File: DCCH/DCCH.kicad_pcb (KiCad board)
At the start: 4 copper layers, 139.7 x 88.9 mm, 30 parts, among them J1 Conn_01x02, J2 Conn_01x02, J3 Conn_01x05, J4 Conn_01x05, J5 Conn_02x08_Odd_Even, U11 SN74HC595, U12 SN74HC595, U13 SN74HC595, U14 SN74HC595, U21 SN754410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

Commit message: Added a layer number indicator.
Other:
- board text added: "1"
- board text added: "2"
- board text added: "3"
- board text added: "4"
- board text added: "LAYER"

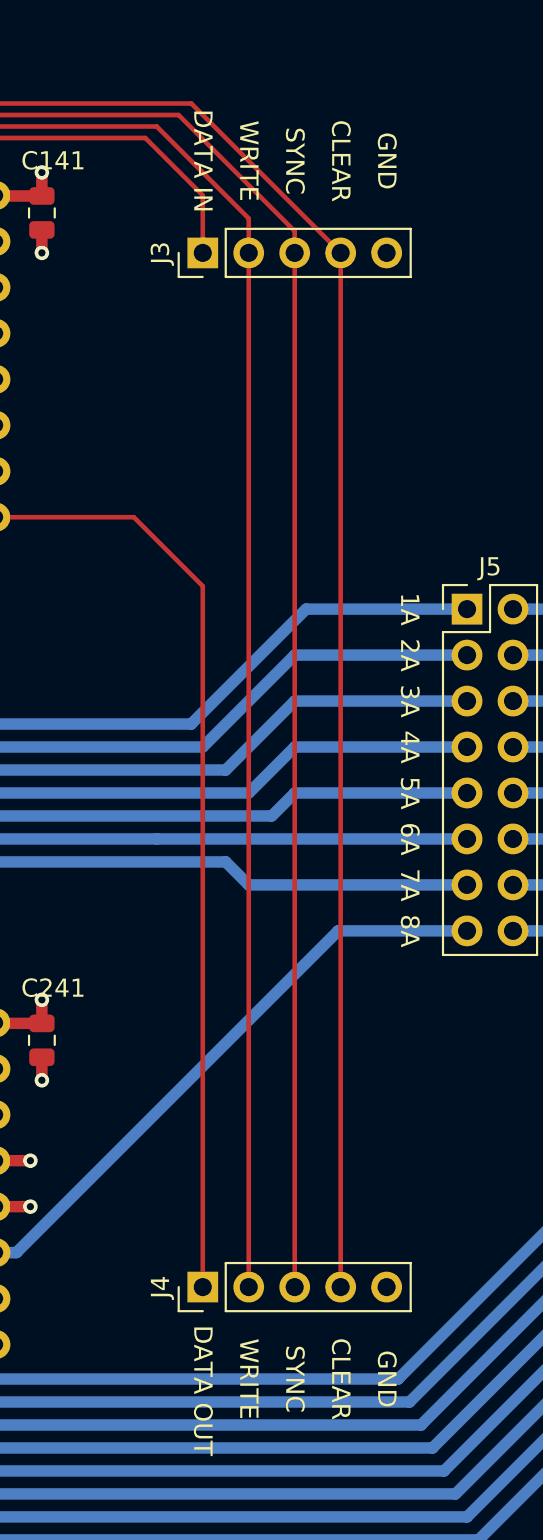
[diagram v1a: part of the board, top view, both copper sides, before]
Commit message: Fixed WRITE and SYNC pins, as they were mixed up.
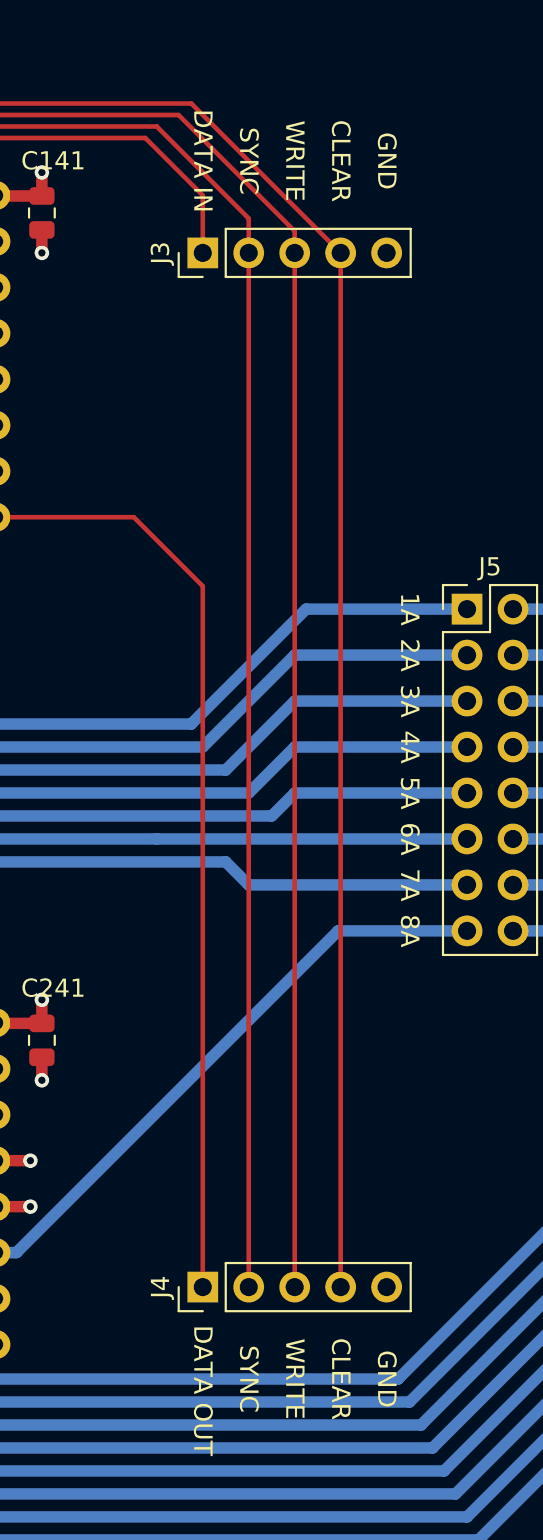
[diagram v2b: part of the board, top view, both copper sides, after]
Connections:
- J3 pad 2: WRITE -> SYNC
- J3 pad 3: SYNC -> WRITE
- J4 pad 2: WRITE -> SYNC
- J4 pad 3: SYNC -> WRITE
- U11 pad 11: SYNC -> WRITE
- U11 pad 12: WRITE -> SYNC
- U12 pad 11: SYNC -> WRITE
- U12 pad 12: WRITE -> SYNC
- U13 pad 11: SYNC -> WRITE
- U13 pad 12: WRITE -> SYNC
- U14 pad 11: SYNC -> WRITE
- U14 pad 12: WRITE -> SYNC
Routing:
- net WRITE: track 211.4 -> 217.5 mm
- net SYNC: track 217.5 -> 211.4 mm

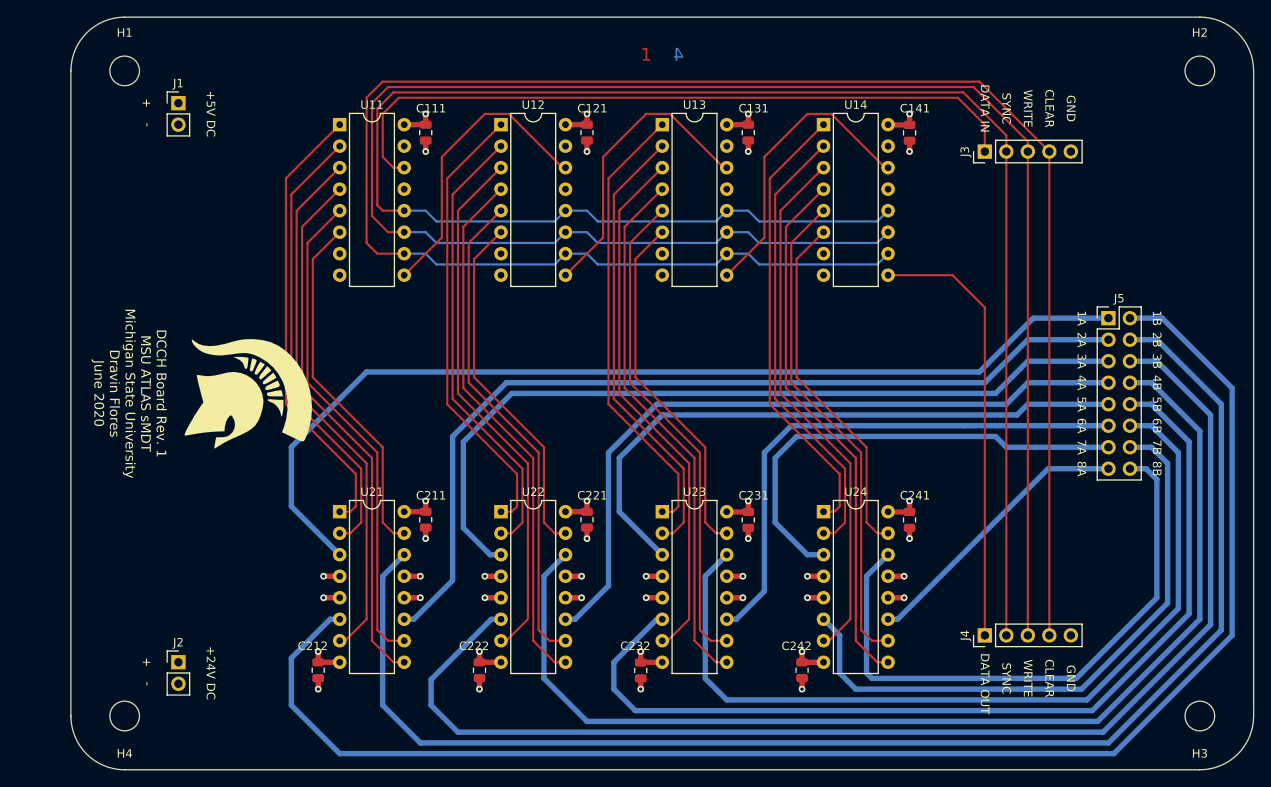
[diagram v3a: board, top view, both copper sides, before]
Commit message: Changed board layout once again. Updated schematic. Updated board.
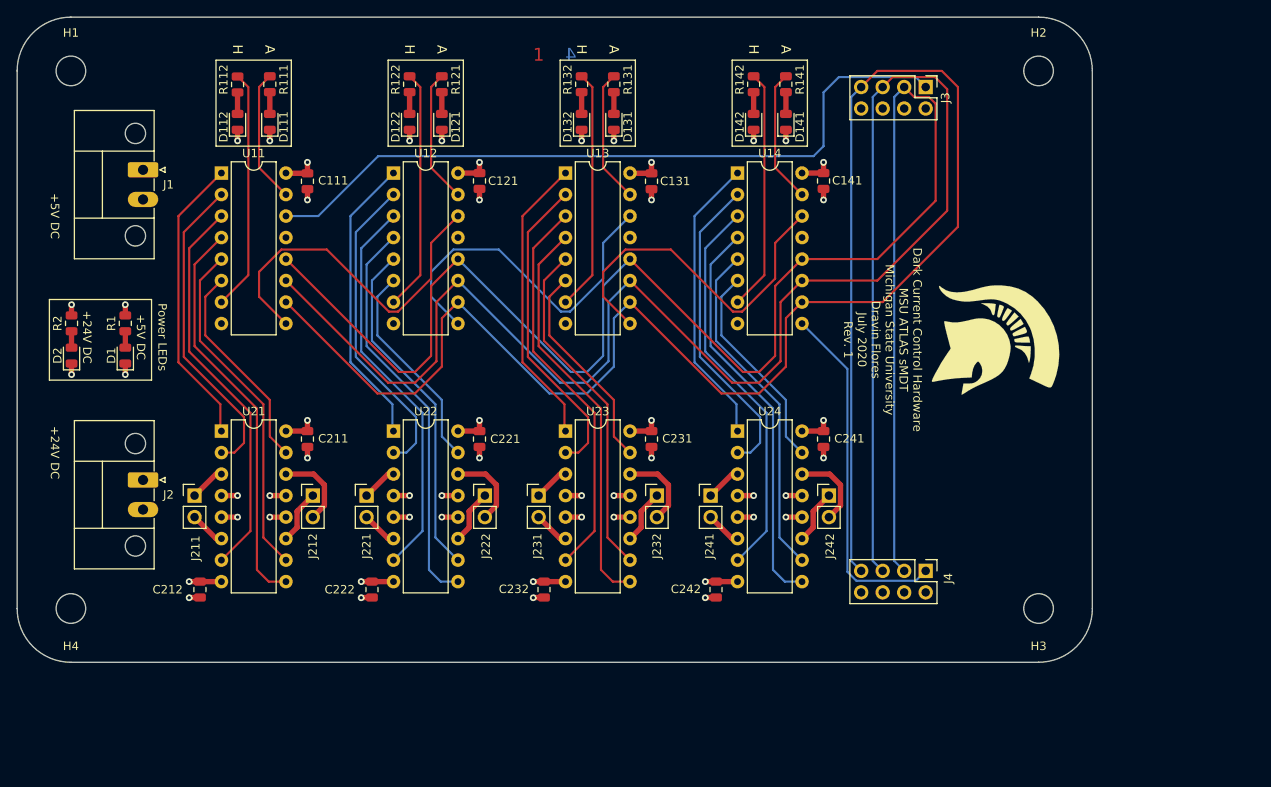
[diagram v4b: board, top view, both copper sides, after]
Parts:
- removed J5: Conn_02x08_Odd_Even, Connector_PinHeader_2.54mm:PinHeader_2x08_P2.54mm_Vertical
- added D1: LED, LED_SMD:LED_0805_2012Metric, F.Cu at (76.3, 78.1)
- added D111: LED, LED_SMD:LED_0805_2012Metric, F.Cu at (93.3, 50.5)
- added D112: LED, LED_SMD:LED_0805_2012Metric, F.Cu at (89.5, 50.5)
- added D121: LED, LED_SMD:LED_0805_2012Metric, F.Cu at (113.7, 50.5)
- added D122: LED, LED_SMD:LED_0805_2012Metric, F.Cu at (109.9, 50.5)
- added D131: LED, LED_SMD:LED_0805_2012Metric, F.Cu at (134.0, 50.5)
- added D132: LED, LED_SMD:LED_0805_2012Metric, F.Cu at (130.2, 50.5)
- added D141: LED, LED_SMD:LED_0805_2012Metric, F.Cu at (154.3, 50.5)
- added D142: LED, LED_SMD:LED_0805_2012Metric, F.Cu at (150.5, 50.5)
- added D2: LED, LED_SMD:LED_0805_2012Metric, F.Cu at (69.9, 78.1)
- added J211: Conn_01x02, Connector_PinHeader_2.54mm:PinHeader_1x02_P2.54mm_Vertical, F.Cu at (84.5, 94.6)
- added J212: Conn_01x02, Connector_PinHeader_2.54mm:PinHeader_1x02_P2.54mm_Vertical, F.Cu at (98.4, 94.6)
- added J221: Conn_01x02, Connector_PinHeader_2.54mm:PinHeader_1x02_P2.54mm_Vertical, F.Cu at (104.8, 94.6)
- added J222: Conn_01x02, Connector_PinHeader_2.54mm:PinHeader_1x02_P2.54mm_Vertical, F.Cu at (118.7, 94.6)
- added J231: Conn_01x02, Connector_PinHeader_2.54mm:PinHeader_1x02_P2.54mm_Vertical, F.Cu at (125.1, 94.6)
- added J232: Conn_01x02, Connector_PinHeader_2.54mm:PinHeader_1x02_P2.54mm_Vertical, F.Cu at (139.1, 94.6)
- added J241: Conn_01x02, Connector_PinHeader_2.54mm:PinHeader_1x02_P2.54mm_Vertical, F.Cu at (145.4, 94.6)
- added J242: Conn_01x02, Connector_PinHeader_2.54mm:PinHeader_1x02_P2.54mm_Vertical, F.Cu at (159.4, 94.6)
- added R1: R_US, Resistor_SMD:R_0805_2012Metric, F.Cu at (76.3, 74.3)
- added R111: R_US, Resistor_SMD:R_0805_2012Metric, F.Cu at (93.3, 46.0)
- added R112: R_US, Resistor_SMD:R_0805_2012Metric, F.Cu at (89.5, 46.1)
- added R121: R_US, Resistor_SMD:R_0805_2012Metric, F.Cu at (113.7, 46.0)
- added R122: R_US, Resistor_SMD:R_0805_2012Metric, F.Cu at (109.9, 46.0)
- added R131: R_US, Resistor_SMD:R_0805_2012Metric, F.Cu at (134.0, 46.0)
- added R132: R_US, Resistor_SMD:R_0805_2012Metric, F.Cu at (130.2, 46.0)
- added R141: R_US, Resistor_SMD:R_0805_2012Metric, F.Cu at (154.3, 46.0)
- added R142: R_US, Resistor_SMD:R_0805_2012Metric, F.Cu at (150.5, 46.0)
- added R2: R_US, Resistor_SMD:R_0805_2012Metric, F.Cu at (69.9, 74.3)
- J1, J2: footprint Connector_PinHeader_2.54mm:PinHeader_1x02_P2.54mm_Vertical -> Connector_Phoenix_MC:PhoenixContact_MC_1,5_2-GF-3.5_1x02_P3.50mm_Horizontal_ThreadedFlange_MountHole
- J3, J4: value Conn_01x05 -> Conn_02x04_Odd_Even; footprint Connector_PinHeader_2.54mm:PinHeader_1x05_P2.54mm_Vertical -> Connector_PinHeader_2.54mm:PinHeader_2x04_P2.54mm_Vertical
- moved G*** 88.5 mm to (179.1, 76.2)
- moved H3 22.9 mm to (184.2, 108.0)
- moved J2 21.9 mm to (78.4, 92.8), turned to 270 degrees
- moved H2 19.0 mm to (184.2, 44.5)
- moved C211 16.9 mm to (97.8, 87.9)
- moved C212 16.9 mm to (85.1, 105.7)
- moved U21 16.9 mm to (87.6, 87.0)
- moved C221 15.9 mm to (118.1, 87.9)
- moved C222 15.9 mm to (105.4, 105.7)
- moved U22 15.9 mm to (108.0, 87.0)
- moved C111 15.1 mm to (97.8, 57.5)
- moved U11 15.1 mm to (87.6, 56.5)
- moved C231 14.9 mm to (138.4, 87.9)
- moved C232 14.9 mm to (125.7, 105.7)
- moved U23 14.9 mm to (128.3, 87.0)
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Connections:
- J3 pad 2: SYNC -> GND
- J3 pad 3: WRITE -> SYNC
- J3 pad 4: CLEAR -> GND
- J3 pad 5: GND -> WRITE
- J4 pad 2: SYNC -> GND
- J4 pad 3: WRITE -> SYNC
- J4 pad 4: CLEAR -> GND
- J4 pad 5: GND -> WRITE
- U11 pad 15: (no net) -> CON-11A
- U11 pad 7: (no net) -> CON-11H
- U12 pad 15: (no net) -> CON-12A
- U12 pad 7: (no net) -> CON-12H
- U13 pad 15: (no net) -> CON-13A
- U13 pad 7: (no net) -> CON-13H
- U14 pad 15: (no net) -> CON-14A
- U14 pad 7: (no net) -> CON-14H
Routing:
- net OUT-1B: track 177.2 -> 4.23 mm
- net OUT-2B: track 165.9 -> 9.44 mm
- net OUT-3B: track 149.8 -> 4.23 mm
- net OUT-4B: track 133.1 -> 9.44 mm
- net OUT-1A: track 117.9 -> 4.23 mm
- net OUT-5B: track 113.9 -> 4.23 mm
- net OUT-2A: track 106.8 -> 6.40 mm
- net OUT-6B: track 102.5 -> 9.44 mm
- net OUT-3A: track 96.1 -> 4.23 mm
- net OUT-4A: track 84.9 -> 6.40 mm
- net OUT-5A: track 73.9 -> 4.23 mm
- net OUT-7B: track 72.6 -> 4.23 mm
- net OUT-8B: track 71.2 -> 9.44 mm
- net OUT-6A: track 64.1 -> 6.40 mm
- net OUT-7A: track 55.9 -> 4.23 mm
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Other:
- board size 139.7 x 88.9 mm -> 127 x 76.2 mm
- board text added: "A"
- board text added: "Dark Current Control Hardware MSU ATLAS sMDT Michigan State University Dravin Flores July 2020 Rev. 1"
- board text added: "H"
- board text added: "Power LEDs"
- board text removed: "+"
- board text removed: "-"
- board text removed: "1A"
- board text removed: "1B"
- board text removed: "2A"
- board text removed: "2B"
- board text removed: "3A"
- board text removed: "3B"
- board text removed: "4A"
- board text removed: "4B"
- board text removed: "5A"
- board text removed: "5B"
- board text removed: "6A"
- board text removed: "6B"
- board text removed: "7A"
- board text removed: "7B"
- board text removed: "8A"
- board text removed: "8B"
- board text removed: "CLEAR"
- board text removed: "DATA IN"
- board text removed: "DATA OUT"
- board text removed: "DCCH Board Rev. 1 MSU ATLAS sMDT Michigan State University Dravin Flores June 2020"
- board text removed: "GND"
- board text removed: "SYNC"
- board text removed: "WRITE"

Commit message: Added plots and fixed silk screen.
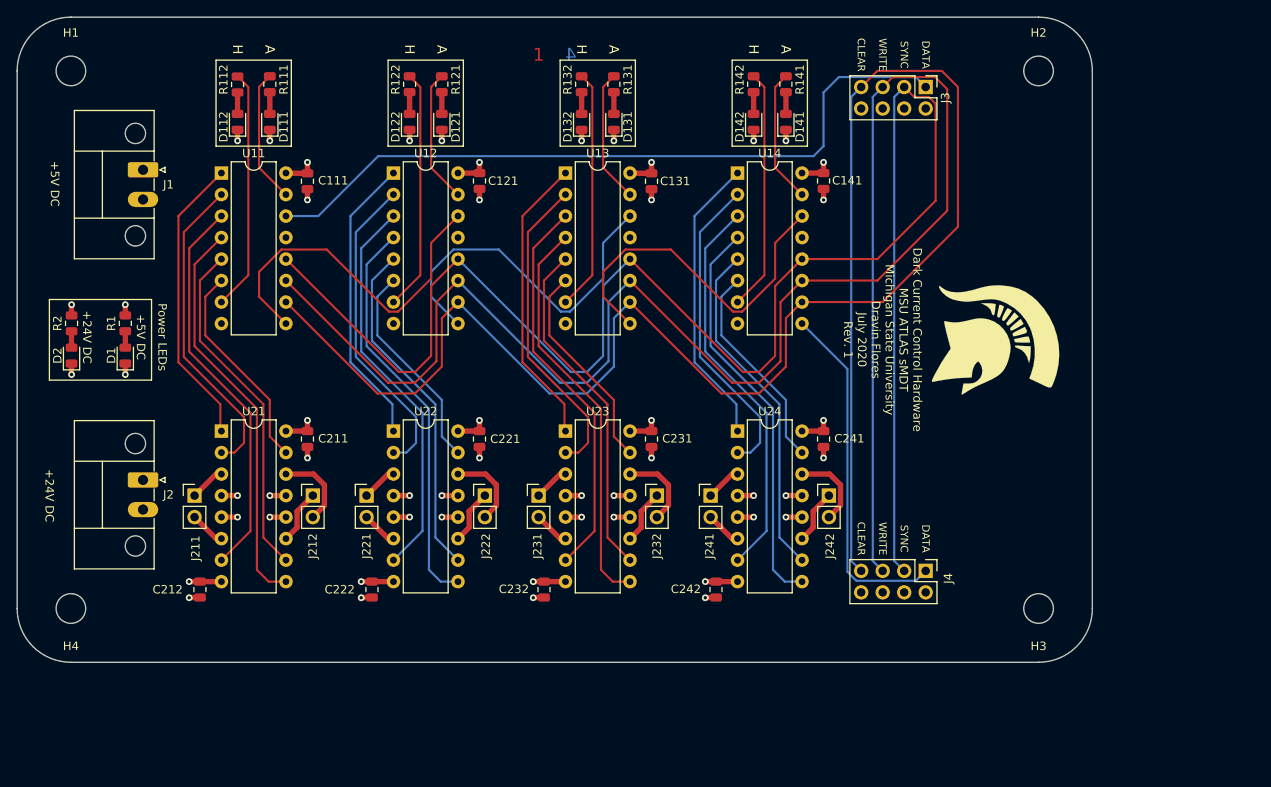
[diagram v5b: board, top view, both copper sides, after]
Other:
- board text added: "CLEAR"
- board text added: "DATA"
- board text added: "SYNC"
- board text added: "WRITE"
